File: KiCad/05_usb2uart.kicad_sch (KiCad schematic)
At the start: 18 parts, among them IC501 FT232RL-REEL, J501 Conn_01x09_Pin, J502 Conn_01x09_Pin, J503 Conn_01x06_Pin, J504 USB_C_Receptacle_USB2.0_16P, U501 USBLC6-2SC6

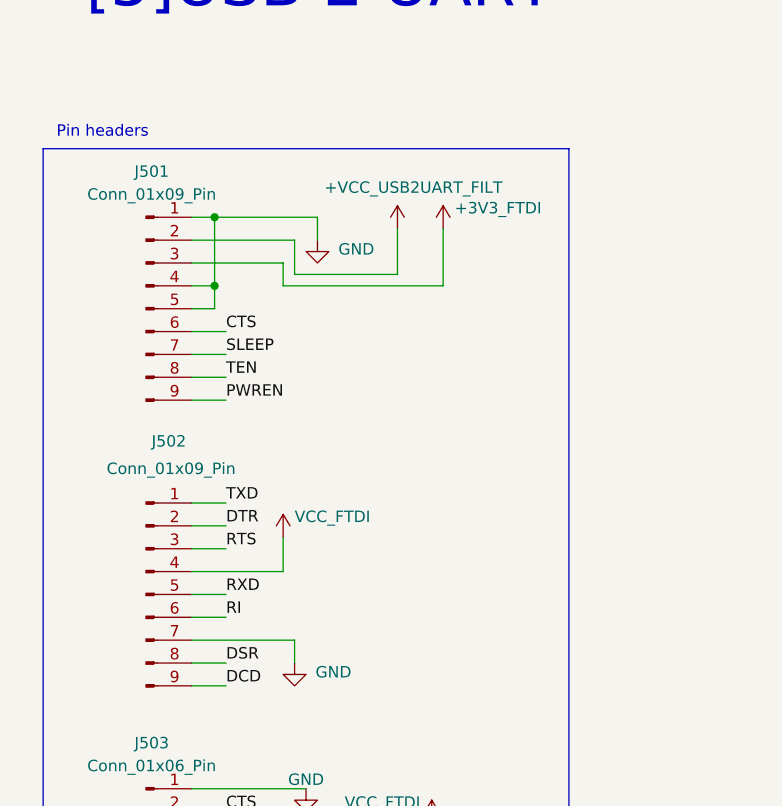
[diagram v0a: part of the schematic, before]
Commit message: FTDI signals routing
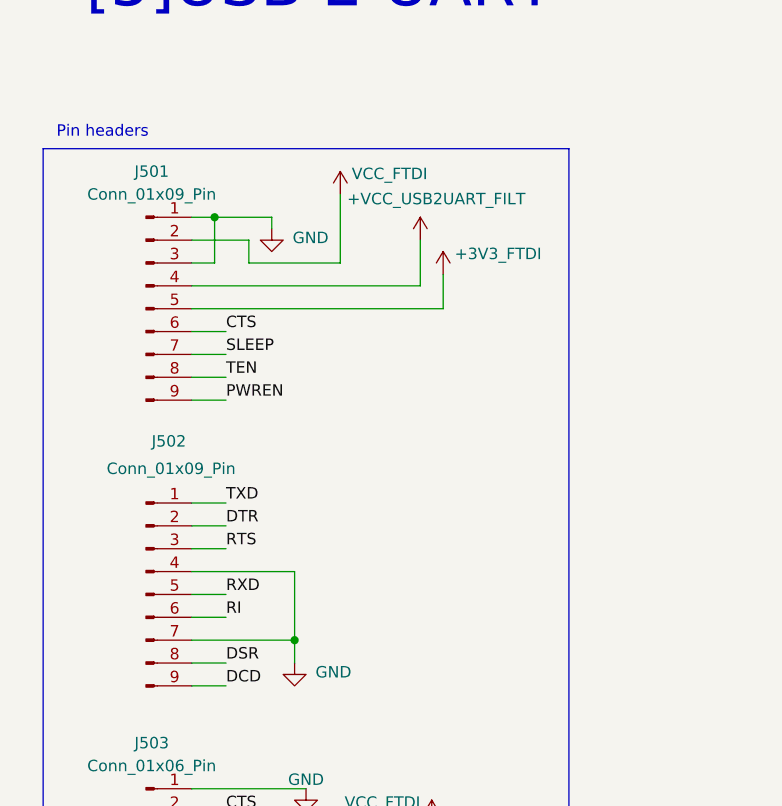
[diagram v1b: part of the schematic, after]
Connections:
- net +3V3_FTDI: now also J501.5 (Pin_5); no longer J501.3 (Pin_3)
- net +VCC_USB2UART_FILT: now also J501.4 (Pin_4); no longer J501.2 (Pin_2)
- net GND: now also J501.3 (Pin_3), J502.4 (Pin_4); no longer J501.4 (Pin_4), J501.5 (Pin_5)
- net VCC_FTDI: now also J501.2 (Pin_2); no longer J502.4 (Pin_4)

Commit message: Fill BOM table
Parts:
- C501, C503: footprint Capacitor_SMD:C_0805_2012Metric -> Capacitor_SMD:C_0603_1608Metric; Manufacturer Part Number (none) -> CL10A226MP8NUNE; Manufacturer Product Number CL21A226MQQNNNE -> (none)
- IC501: Manufacturer (none) -> FTDI Chip; Manufacturer Part Number (none) -> FT232RL-REEL; Manufacturer_Name FTDI Chip -> (none); Manufacturer_Part_Number FT232RL-REEL -> (none); Mouser Part Number 895-FT232RL -> (none); Mouser Price/Stock https://www.mouser.co.uk/ProductDetail/FTDI/FT232RL-REEL?qs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 -> (none)
- R501, R502: LCSC link https://www.lcsc.com/product-detail/Chip-Resistor-Surface-M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 -> (none)
- R505: footprint Resistor_SMD:R_0603_1608Metric -> Resistor_SMD:R_0402_1005Metric; Manufacturer Part Number 0603WAF1004T5E -> 0402WGF1004TCE
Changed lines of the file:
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@@
-			)
-		)
-		(property "LCSC link" "https://www.lcsc.com/product-detail/Chip-Resistor-Surface-Mount_UNI-ROYAL-Uniroyal-Elec-0402WGF5101TCE_C25905.html"
-			(at 201.93 104.14 0)
-			(effects
-				(font
-					(size 1.27 1.27)
-				)
-				(hide yes)
 			)
 		)
@@
 			)
 		)
-		(property "LCSC link" "https://www.lcsc.com/product-detail/Chip-Resistor-Surface-Mount_UNI-ROYAL-Uniroyal-Elec-0402WGF5101TCE_C25905.html"
-			(at 193.04 104.14 0)
-			(effects
-				(font
-					(size 1.27 1.27)
-				)
-				(hide yes)
-			)
-		)
 		(property "Manufacturer" "UNI-ROYAL(Uniroyal Elec)"
 			(at 193.04 104.14 0)
@@
 			)
 		)
-		(property "Footprint" "Capacitor_SMD:C_0805_2012Metric"
+		(property "Footprint" "Capacitor_SMD:C_0603_1608Metric"
 			(at 110.1852 55.88 0)
 			(effects
@@
 			)
 		)
-		(property "Manufacturer Product Number" "CL21A226MQQNNNE"
+		(property "Manufacturer Part Number" "CL10A226MP8NUNE"
 			(at 109.22 52.07 0)
 			(effects
@@
 			)
 		)
-		(property "Manufacturer_Name" "FTDI Chip"
-			(at 118.11 587.63 0)
-			(effects
-				(font
-					(size 1.27 1.27)
-				)
-				(justify left top)
-				(hide yes)
-			)
-		)
-		(property "Manufacturer_Part_Number" "FT232RL-REEL"
-			(at 118.11 687.63 0)
-			(effects
-				(font
-					(size 1.27 1.27)
-				)
-				(justify left top)
-				(hide yes)
-			)
-		)
-		(property "Mouser Part Number" "895-FT232RL"
-			(at 118.11 787.63 0)
-			(effects
-				(font
-					(size 1.27 1.27)
-				)
-				(justify left top)
-				(hide yes)
-			)
-		)
-		(property "Mouser Price/Stock" "https://www.mouser.co.uk/ProductDetail/FTDI/FT232RL-REEL?qs=D1%2FPMqvA103RC6OU6bKtoA%3D%3D"
-			(at 118.11 887.63 0)
-			(effects
-				(font
-					(size 1.27 1.27)
-				)
-				(justify left top)
-				(hide yes)
-			)
-		)
 		(property "Arrow Part Number" "FT232RL-REEL"
 			(at 118.11 987.63 0)
@@
 				)
 				(justify left top)
+				(hide yes)
+			)
+		)
+		(property "Manufacturer" "FTDI Chip"
+			(at 147.32 92.71 0)
+			(effects
+				(font
+					(size 1.27 1.27)
+				)
+				(hide yes)
+			)
+		)
+		(property "Manufacturer Part Number" "FT232RL-REEL"
+			(at 147.32 92.71 0)
+			(effects
+				(font
+					(size 1.27 1.27)
+				)
 				(hide yes)
 			)
@@
 			)
 		)
-		(property "Footprint" "Capacitor_SMD:C_0805_2012Metric"
+		(property "Footprint" "Capacitor_SMD:C_0603_1608Metric"
 			(at 110.1852 82.55 0)
 			(effects
@@
 			)
 		)
-		(property "Manufacturer Product Number" "CL21A226MQQNNNE"
+		(property "Manufacturer Part Number" "CL10A226MP8NUNE"
 			(at 109.22 78.74 0)
 			(effects
@@
 			)
 		)
-		(property "Footprint" "Resistor_SMD:R_0603_1608Metric"
+		(property "Footprint" "Resistor_SMD:R_0402_1005Metric"
 			(at 31.75 174.498 90)
 			(effects
@@
 			)
 		)
-		(property "Manufacturer Part Number" "0603WAF1004T5E"
+		(property "Manufacturer Part Number" "0402WGF1004TCE"
 			(at 31.75 172.72 90)
 			(effects

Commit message: Production files
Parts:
- R505: value DNP, 1MR -> 1MR
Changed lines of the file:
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@@
 			)
 		)
-		(property "Value" "DNP, 1MR"
+		(property "Value" "1MR"
 			(at 31.496 175.006 90)
 			(effects

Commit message: BOM updates
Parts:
- R501, R502, R503, R504: Manufacturer UNI-ROYAL(Uniroyal Elec) -> UNI-ROYAL
- R505: value 1MR -> 910kR; Manufacturer UNI-ROYAL(Uniroyal Elec) -> UNI-ROYAL; Manufacturer Part Number 0402WGF1004TCE -> 0402WGJ0914TCE
- U501: Manufacturer STMicroelectronics -> ST
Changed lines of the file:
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@@
 			)
 		)
-		(property "Manufacturer" "UNI-ROYAL(Uniroyal Elec)"
+		(property "Manufacturer" "UNI-ROYAL"
 			(at 201.93 104.14 0)
 			(effects
@@
 			)
 		)
-		(property "Manufacturer" "UNI-ROYAL(Uniroyal Elec)"
+		(property "Manufacturer" "UNI-ROYAL"
 			(at 193.04 104.14 0)
 			(effects
@@
 			)
 		)
-		(property "Manufacturer" "UNI-ROYAL(Uniroyal Elec)"
+		(property "Manufacturer" "UNI-ROYAL"
 			(at 39.37 151.13 0)
 			(effects
@@
 			)
 		)
-		(property "Manufacturer" "STMicroelectronics"
+		(property "Manufacturer" "ST"
 			(at 182.88 119.38 0)
 			(effects
@@
 			)
 		)
-		(property "Value" "1MR"
+		(property "Value" "910kR"
 			(at 31.496 175.006 90)
 			(effects
@@
 			)
 		)
-		(property "Manufacturer" "UNI-ROYAL(Uniroyal Elec)"
+		(property "Manufacturer" "UNI-ROYAL"
 			(at 31.75 172.72 90)
 			(effects
@@
 			)
 		)
-		(property "Manufacturer Part Number" "0402WGF1004TCE"
+		(property "Manufacturer Part Number" "0402WGJ0914TCE"
 			(at 31.75 172.72 90)
 			(effects
@@
 			)
 		)
-		(property "Manufacturer" "UNI-ROYAL(Uniroyal Elec)"
+		(property "Manufacturer" "UNI-ROYAL"
 			(at 39.37 144.78 0)
 			(effects
